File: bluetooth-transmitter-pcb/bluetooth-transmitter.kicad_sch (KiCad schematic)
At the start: 16 parts, among them J1 Boot option, J2 Flash UART, SW1 Reset, SW2 RotaryEncoder_Switch, U1 ESP32-WROOM-32

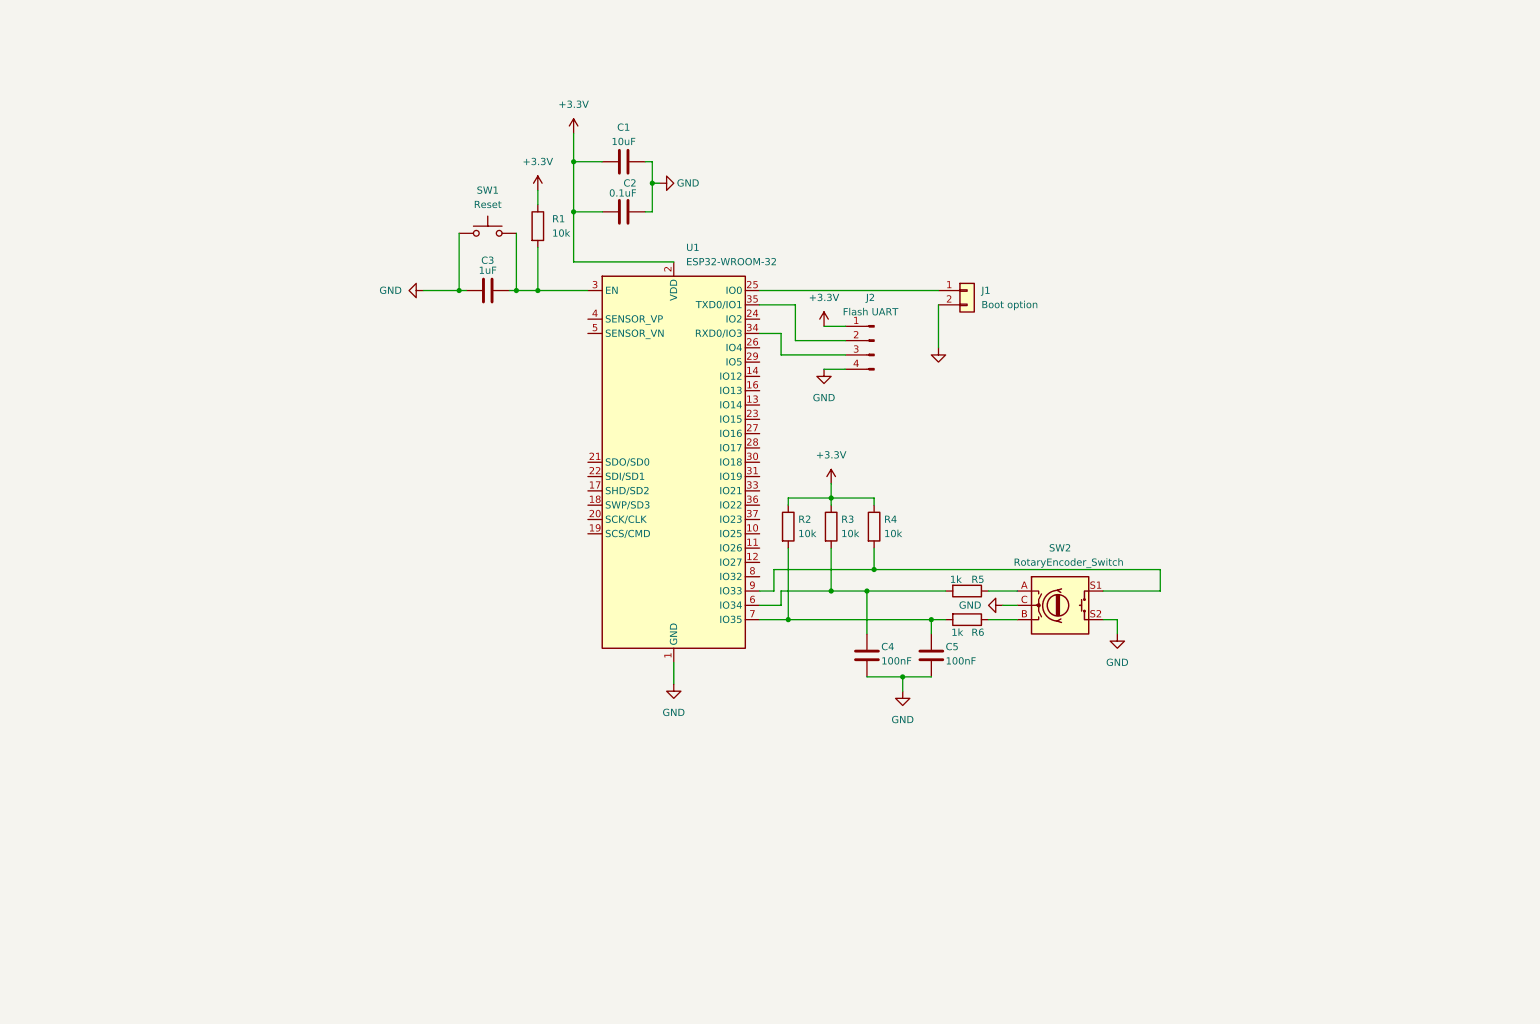
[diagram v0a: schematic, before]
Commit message: Update PCB to last version
Add power chain and PCM1808 to schematic. Create PCB from shecmatic.
Make PCB ready for production.
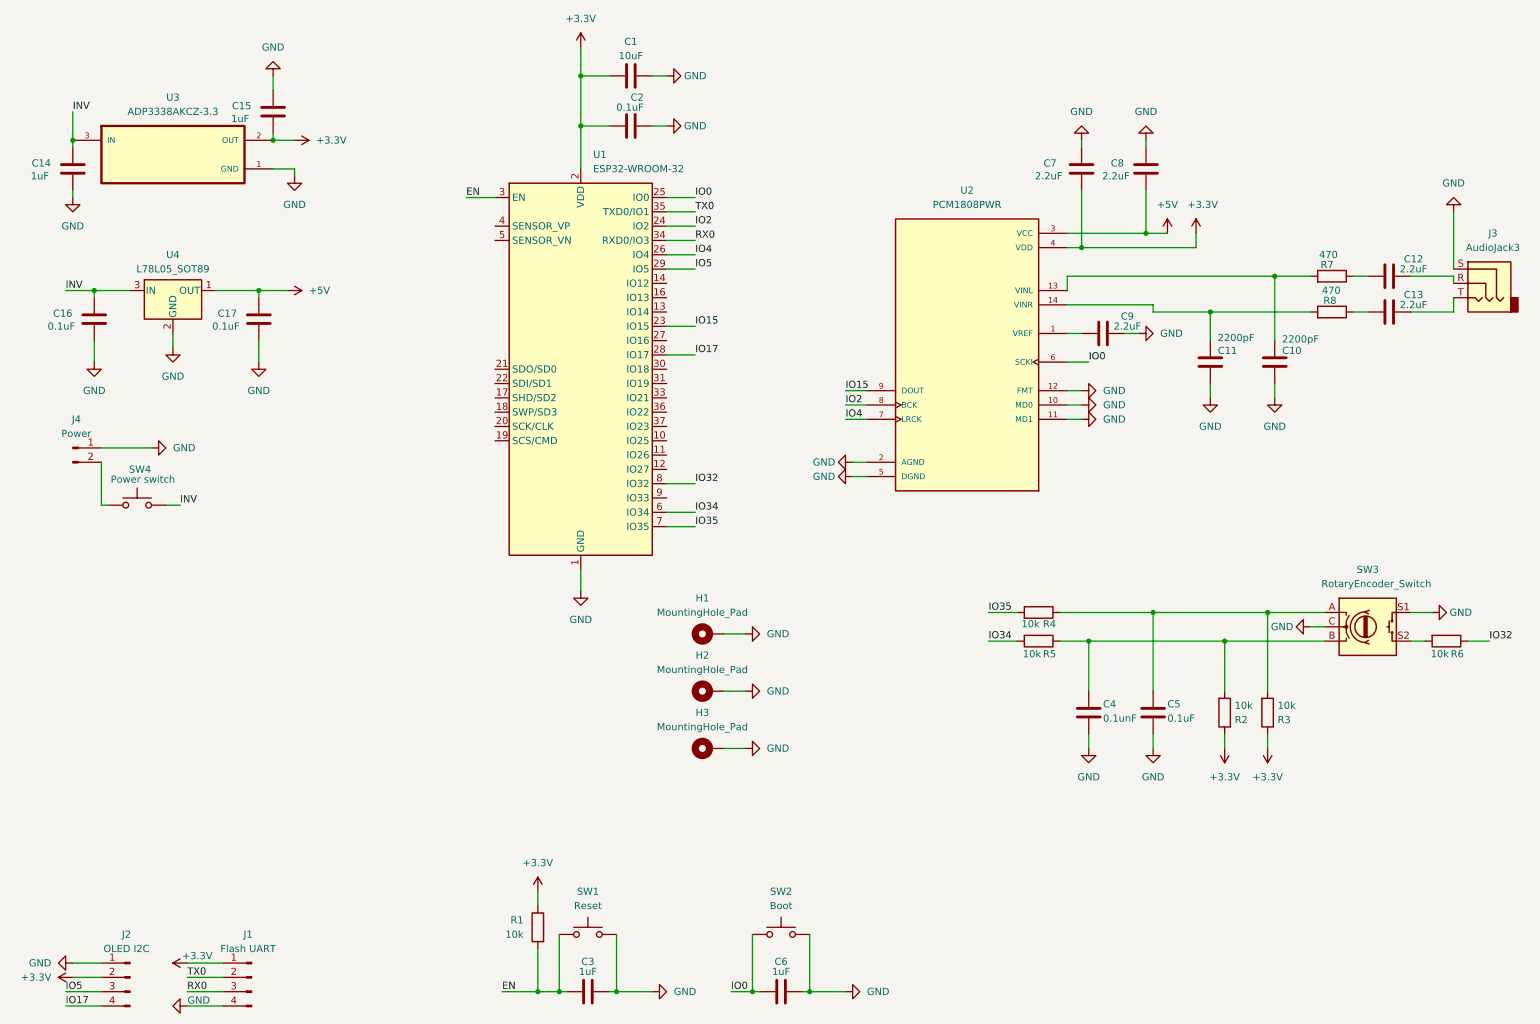
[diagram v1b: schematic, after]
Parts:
- removed J1: Boot option, Connector_PinHeader_2.54mm:PinHeader_1x02_P2.54mm_Vertical, symbol Connector_Generic:Conn_01x02
- removed R4: 10k, Resistor_SMD:R_1206_3216Metric_Pad1.30x1.75mm_HandSolder, symbol Device:R
- added C10, C11: 2200pF, Capacitor_SMD:C_0603_1608Metric_Pad1.08x0.95mm_HandSolder, symbol Device:C
- added C12, C13, C7, C8, C9: 2.2uF, Capacitor_SMD:C_0603_1608Metric_Pad1.08x0.95mm_HandSolder, symbol Device:C
- added C14, C15, C6: 1uF, Capacitor_SMD:C_0603_1608Metric_Pad1.08x0.95mm_HandSolder, symbol Device:C
- added C16, C17: 0.1uF, Capacitor_SMD:C_0603_1608Metric_Pad1.08x0.95mm_HandSolder, symbol Device:C
- added H1, H2, H3: MountingHole_Pad, MountingHole:MountingHole_2.2mm_M2_ISO7380_Pad_TopOnly, symbol Mechanical:MountingHole_Pad
- added J2: OLED I2C, Connector_PinHeader_2.54mm:PinHeader_1x04_P2.54mm_Vertical, symbol Connector:Conn_01x04_Pin
- added J3: AudioJack3, Connector_Audio:Jack_3.5mm_CUI_SJ1-3533NG_Horizontal, symbol Connector_Audio:AudioJack3
- added J4: Power, Connector_PinSocket_2.54mm:PinSocket_1x02_P2.54mm_Vertical, symbol Connector:Conn_01x02_Pin
- added R6: 10k, Resistor_SMD:R_1206_3216Metric_Pad1.30x1.75mm_HandSolder, symbol Device:R
- added R7, R8: 470, Resistor_SMD:R_1206_3216Metric_Pad1.30x1.75mm_HandSolder, symbol Device:R
- added SW2: Boot, Button_Switch_THT:SW_PUSH_6mm_H4.3mm, symbol Switch:SW_Push
- added SW4: Power switch, Connector_PinSocket_2.54mm:PinSocket_1x02_P2.54mm_Vertical, symbol Switch:SW_Push
- added U2: PCM1808PWR, PCM1808:SOP65P640X120-14N, symbol PCM1808PWR:PCM1808PWR
- added U3: ADP3338AKCZ-3.3, Package_TO_SOT_SMD:SOT-223-3_TabPin2, symbol ADP3338AKCZ-3.3:ADP3338AKCZ-3.3
- added U4: L78L05_SOT89, Package_TO_SOT_SMD:SOT-89-3, symbol Regulator_Linear:L78L05_SOT89
- C4: value 100nF -> 0.1unF
- C5: value 100nF -> 0.1uF
- R4: renamed from R5; value 1k -> 10k
- R5: renamed from R6; value 1k -> 10k
- renumbered J2 to J1, SW2 to SW3
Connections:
- net +3.3V: now also C15.2, C7.2, J2.2 (Pin_2), U2.4 (VDD), U3.2 (OUT)
- net GND: now also SW3.S1, C10.1, C11.1, C14.2, C15.1, C16.2, C17.2, C6.1, C7.1, C8.1, C9.2, H1.1, H2.1, H3.1, J2.1 (Pin_1), J3.S, J4.1 (Pin_1), SW2.1, U2.10 (MD0), U2.11 (MD1), U2.12 (FMT), U2.2 (AGND), U2.5 (DGND), U3.1 (GND), U4.2 (GND); no longer SW3.S2
- net at U1.9 (IO33): no longer SW3.S1
- net EN: now reaches C3.2, R1.2, SW1.2, U1.3 (EN)
- net at R4.1, SW3.A: now also C5.1, R3.2
- net at R5.1, SW3.B: now also C4.1, R2.2
- net IO15: now reaches U1.23 (IO15)
- net IO15: now also U2.9 (DOUT)
- net IO2: now reaches U1.24 (IO2)
- net IO2: now also U2.8 (BCK)
- net IO0: now reaches U1.25 (IO0)
- net IO0: now also C6.2, SW2.2, U2.6 (SCKI)
- net IO4: now reaches U1.26 (IO4)
- net IO4: now also U2.7 (LRCK)
- net IO17: now reaches U1.28 (IO17)
- net IO17: now also J2.4 (Pin_4)
- net IO5: now reaches U1.29 (IO5)
- net IO5: now also J2.3 (Pin_3)
- net RX0: now reaches J1.3 (Pin_3), U1.34 (RXD0/IO3)
- net TX0: now reaches J1.2 (Pin_2), U1.35 (TXD0/IO1)
- net IO32: now reaches U1.8 (IO32)
- net IO32: now also R6.1
- new net: C9.1, U2.1 (VREF)
- new net: C11.2, R8.2, U2.14 (VINR)
- new net: R6.2, SW3.S2
- new net: C12.1, R7.1
- new net: C12.2, J3.R
- new net: J4.2 (Pin_2), SW4.1
- new net: C13.2, J3.T
- new net: C13.1, R8.1
- new net: C10.2, R7.2, U2.13 (VINL)
- new net +5V: C17.1, C8.2, U2.3 (VCC), U4.1 (OUT)
- new net INV: C14.1, C16.1, SW4.2, U3.3 (IN), U4.3 (IN)
- new net IO34: R5.2, U1.6 (IO34)
- new net IO35: R4.2, U1.7 (IO35)
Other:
- moved on the sheet: C1, C2, C3, C4, C5, J1, R1, R2, R3, R4, R5, SW1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
